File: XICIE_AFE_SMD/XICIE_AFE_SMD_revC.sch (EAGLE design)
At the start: 55 parts, among them IC1 LM324D, IC2 CY8C4245T, IC3 AAT1217, J1 22-27-2021-02, Q1 MOSFET-NCHANNELBSS123LT1G, Q2 MOSFET-NCHANNELBSS123LT1G, Q3 MOSFET-NCHANNELBSS123LT1G, Q4 MOSFET-NCHANNELBSS123LT1G, Q5 MOSFET-NCHANNELBSS123LT1G, Q6 MOSFET-NCHANNELBSS123LT1G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

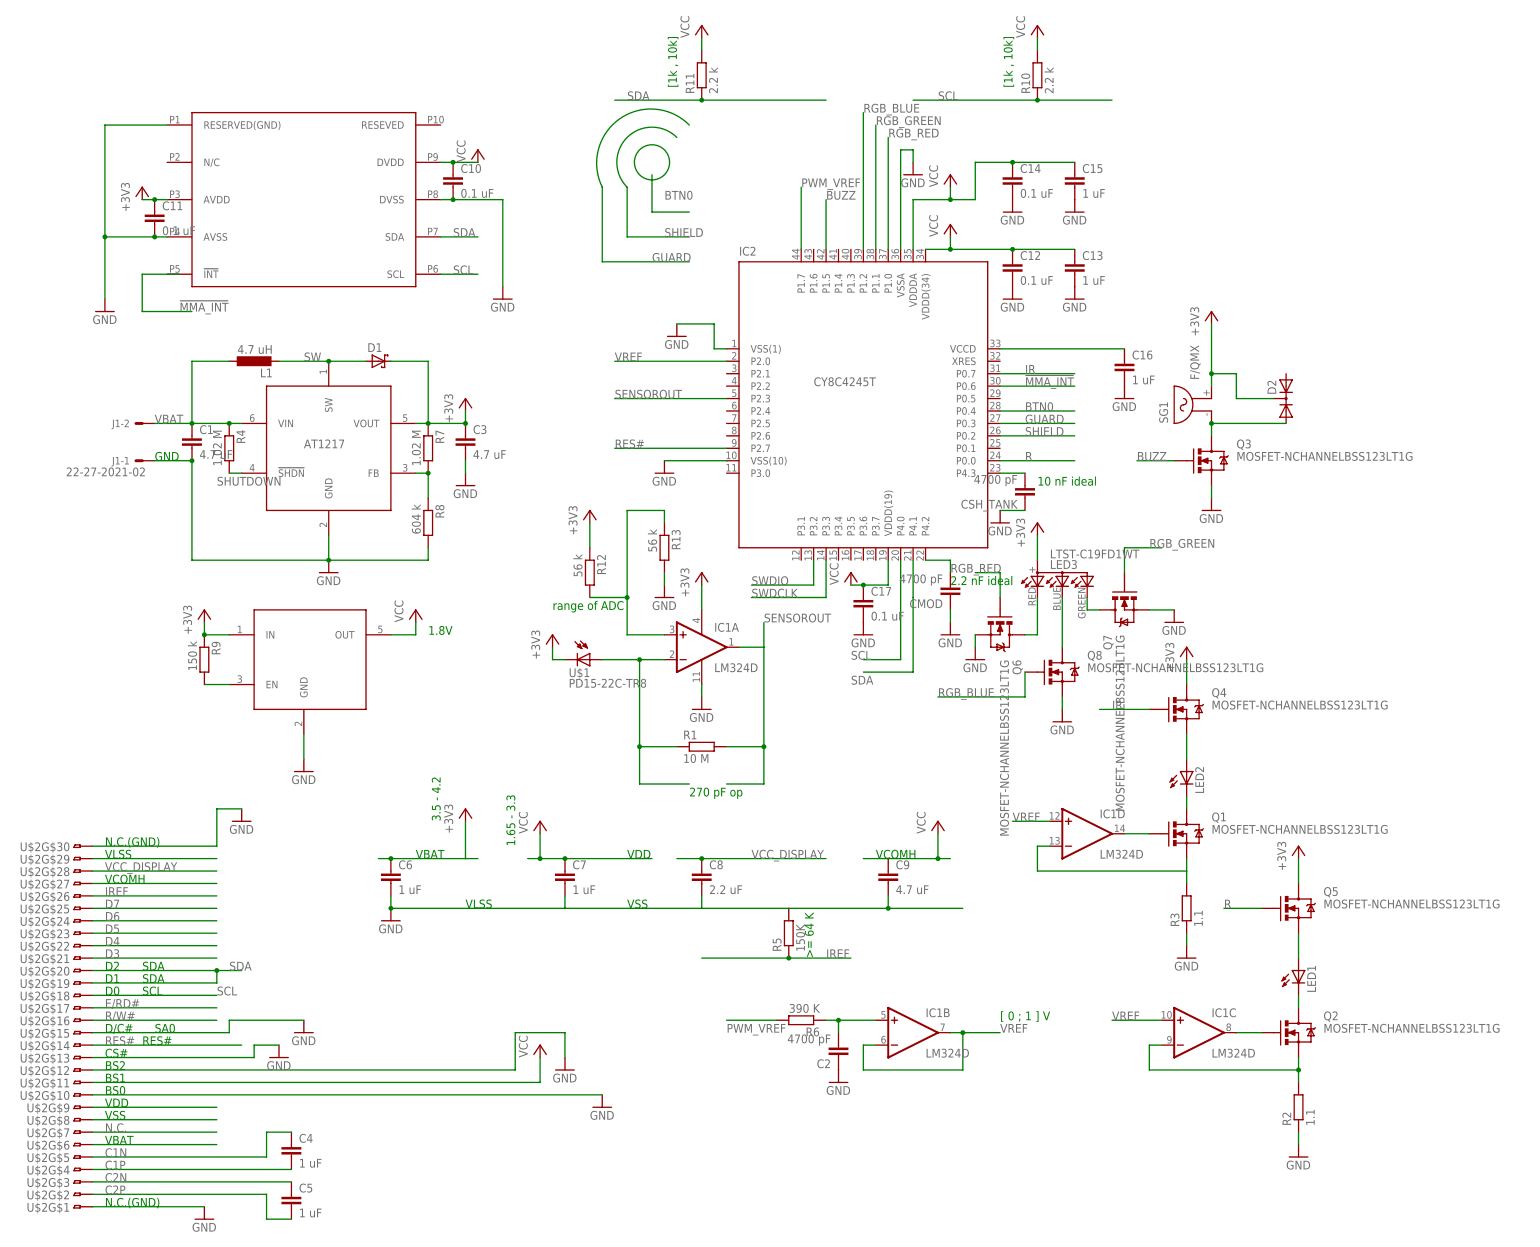
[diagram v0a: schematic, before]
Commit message: Finished rev B of XICIE_AFE_SMD
Many things added, like button, buzzer, RGB
led. Placing improved manually. Still missing
connection to program PSoC4.
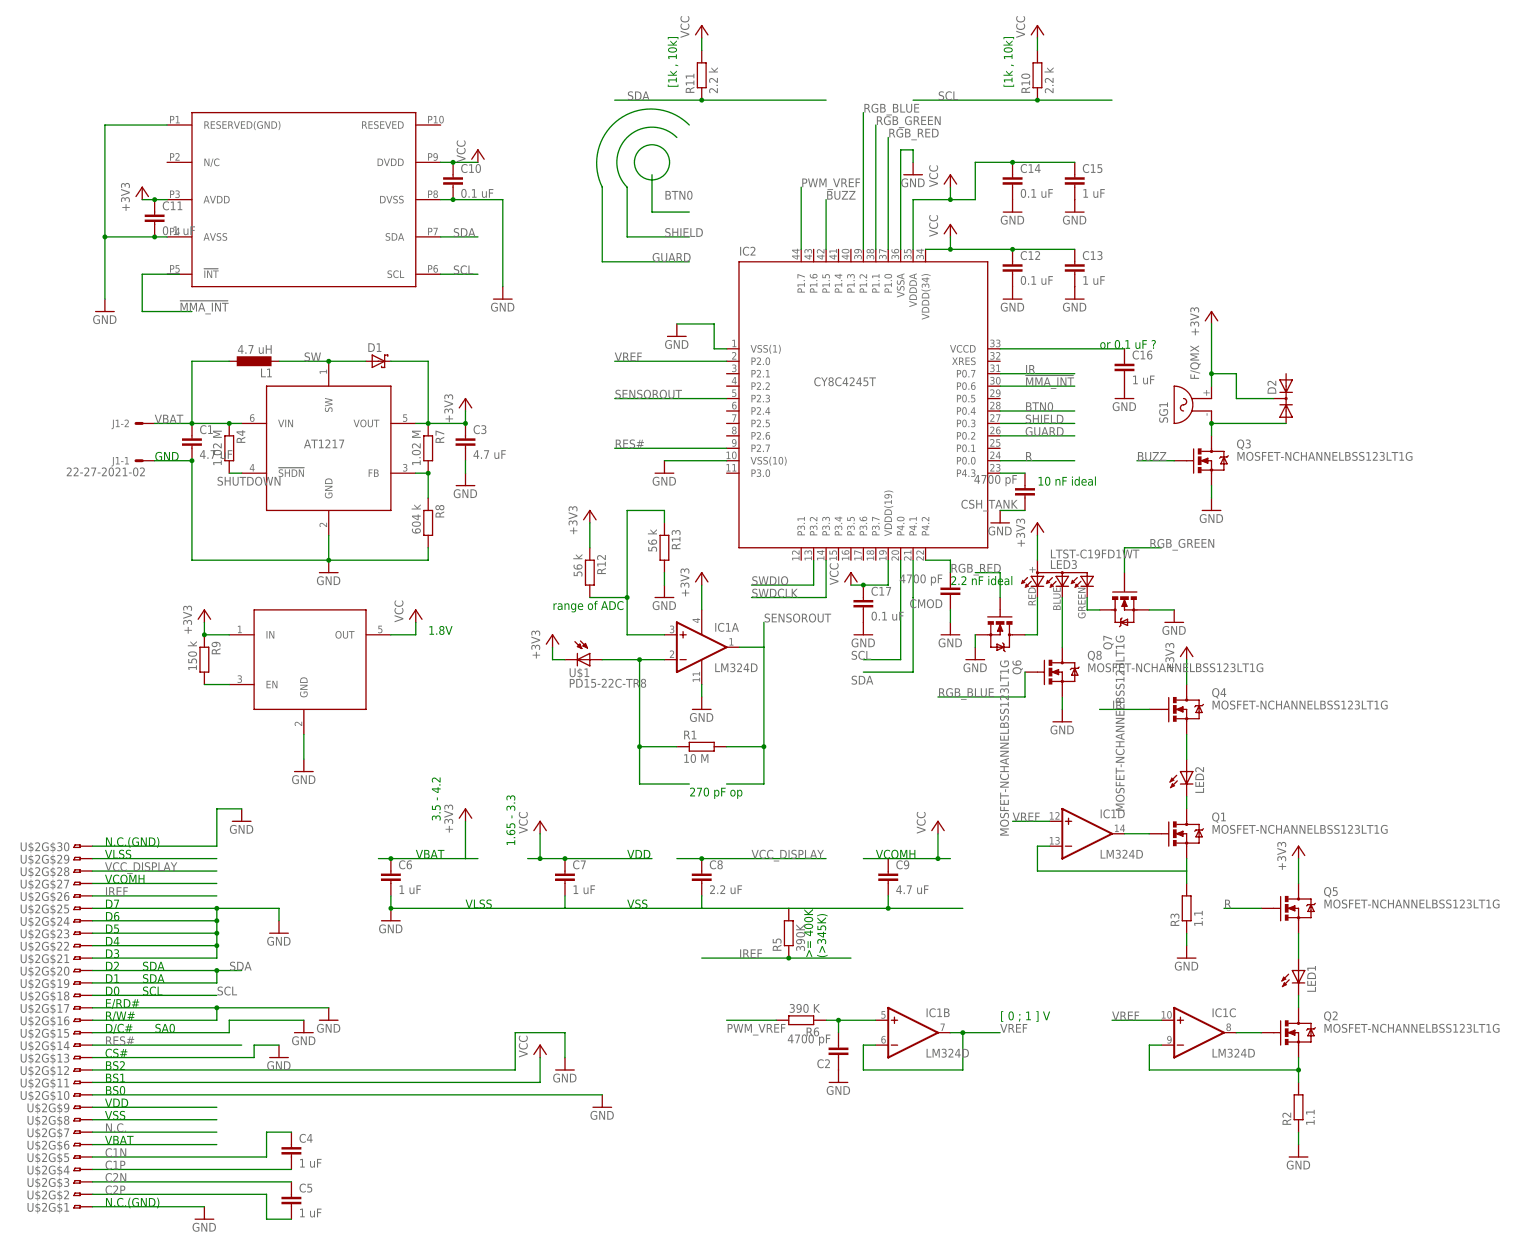
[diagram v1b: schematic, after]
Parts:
- R5: value 150K -> 390K
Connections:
- removed net D3: U$2G$21.1
- removed net D4: U$2G$22.1
- removed net D5: U$2G$23.1
- removed net D6: U$2G$24.1
- removed net D7: U$2G$25.1
- removed net E/RD#: U$2G$17.1
- removed net R/W#: U$2G$16.1
- net GND: now also U$2G$16.1, U$2G$17.1, U$2G$21.1, U$2G$22.1, U$2G$23.1, U$2G$24.1, U$2G$25.1
- net GUARD: now also IC2.P0.2; no longer IC2.P0.3
- net SHIELD: now also IC2.P0.3; no longer IC2.P0.2
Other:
- note added: "D3"
- note added: "D4"
- note added: "D5"
- note added: "D6"
- note added: "D7"
- note added: "E/RD#"
- note added: "R/W#"
- note added: "or 0.1 uF ?"
- note removed: "RES#"
